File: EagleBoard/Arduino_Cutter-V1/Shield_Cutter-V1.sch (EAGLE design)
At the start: 83 parts, among them IC1 L298P, IC2 REG1117, K1 AQY21SOP, K2 AQY21SOP, U1 ARDUINOR3-DIMENSION, X1 2514-, X2 22-23-2041, X3 22-23-2021, X4 22-23-2021

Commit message: Feat: pcb routed
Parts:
- renumbered S1 to RESET
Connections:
- removed net N$25: SV9-1.S
- net BUTTON_INT: now also U1.D2; no longer U1.D3
- net DOWN_BUT: now also D12.C1, R26.2, U1.A1; no longer D11.C2, R25.2, U1.A2
- net E-STOP: now also SV9-1.S
- net LCD_D4: now also X1-8.KL; no longer X1-7.KL
- net LCD_D5: now also X1-7.KL; no longer X1-8.KL
- net LCD_D6: now also X1-10.KL; no longer X1-9.KL
- net LCD_D7: now also X1-9.KL; no longer X1-10.KL
- net RUN_BUT: now also D12.C2, R27.2, U1.A2; no longer D12.C1, R26.2, U1.A3
- net SELECT_BUT: now also D11.C2, R25.2, U1.A3; no longer D12.C2, R27.2, U1.A4/SDA
- net SOL_CUT: now also U1.A4/SDA; no longer U1.A0
- net SOL_PIERCE: now also U1.A5/SCL; no longer U1.A1
- net SPEED_POT: now also U1.A0; no longer U1.A5/SCL
- net STEPER1: now also U1.D10; no longer U1.D13
- net STEPER2: now also U1.D11; no longer U1.D12
- net STEPER3: now also U1.D12; no longer U1.D11
- net STEPER4: now also U1.D13; no longer U1.D10
- net UP_BUT: now also U1.D3; no longer U1.D2

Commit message: Feat: pcb routed
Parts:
- removed U$1: DISCLAIMER, SmartPrj:DISCLAIMER
- D11, D12: value (none) -> 40v
- R24: value (none) -> 10k
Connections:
- net GND: now also IC2.GND
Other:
- moved on the sheet: C1
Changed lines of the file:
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@@
 <part name="GND27" library="supply1" deviceset="GND" device=""/>
 <part name="GND28" library="supply1" deviceset="GND" device=""/>
-<part name="U$1" library="SmartPrj" deviceset="DISCLAIMER" device=""/>
 <part name="SUPPLY3" library="supply1" deviceset="GND" device=""/>
 <part name="SUPPLY1" library="supply1" deviceset="GND" device=""/>
@@
 <part name="P+16" library="supply1" deviceset="+5V" device=""/>
 <part name="R18" library="resistor" deviceset="R-US_" device="R0603" value="10kΩ"/>
-<part name="D11" library="zetex" library_urn="urn:adsk.eagle:library:418" deviceset="D_2C" device="SOT23"/>
-<part name="D12" library="zetex" library_urn="urn:adsk.eagle:library:418" deviceset="D_2C" device="SOT23"/>
+<part name="D11" library="zetex" library_urn="urn:adsk.eagle:library:418" deviceset="D_2C" device="SOT23" value="40v"/>
+<part name="D12" library="zetex" library_urn="urn:adsk.eagle:library:418" deviceset="D_2C" device="SOT23" value="40v"/>
 <part name="P+17" library="supply1" deviceset="+5V" device=""/>
 <part name="R19" library="resistor" deviceset="R-US_" device="M0805" value="10kΩ"/>
@@
 <part name="R21" library="resistor" deviceset="R-US_" device="R0603" value="10kΩ"/>
 <part name="R22" library="resistor" deviceset="R-US_" device="R0603" value="10kΩ"/>
-<part name="R24" library="pot" library_urn="urn:adsk.eagle:library:331" deviceset="TRIM_EU-" device="S64W"/>
+<part name="R24" library="pot" library_urn="urn:adsk.eagle:library:331" deviceset="TRIM_EU-" device="S64W" value="10k"/>
 <part name="P+5" library="supply1" deviceset="+5V" device=""/>
 <part name="GND20" library="supply1" deviceset="GND" device=""/>
@@
 <instance part="GND27" gate="1" x="132.08" y="81.28" rot="R180"/>
 <instance part="GND28" gate="1" x="167.64" y="81.28" rot="R180"/>
-<instance part="U$1" gate="G$1" x="-38.1" y="-104.14"/>
 <instance part="SUPPLY3" gate="1" x="-10.16" y="111.76"/>
 <instance part="SUPPLY1" gate="1" x="-25.4" y="111.76"/>
-<instance part="SUPPLY4" gate="1" x="2.54" y="111.76"/>
+<instance part="SUPPLY4" gate="1" x="5.08" y="111.76"/>
 <instance part="P+4" gate="1" x="17.78" y="132.08" smashed="yes">
 <attribute name="VALUE" x="19.685" y="134.62" size="1.778" layer="96" rot="R180"/>
@@
 </instance>
 <instance part="GND20" gate="1" x="157.48" y="-17.78"/>
-<instance part="C1" gate="G$1" x="2.54" y="121.92" smashed="yes">
-<attribute name="NAME" x="4.064" y="122.301" size="1.778" layer="95"/>
-<attribute name="VALUE" x="4.064" y="117.221" size="1.778" layer="96"/>
+<instance part="C1" gate="G$1" x="5.08" y="121.92" smashed="yes">
+<attribute name="NAME" x="6.604" y="122.301" size="1.778" layer="95"/>
+<attribute name="VALUE" x="6.604" y="117.221" size="1.778" layer="96"/>
 </instance>
 <instance part="C2" gate="G$1" x="17.78" y="121.92" smashed="yes">
@@
 </segment>
 <segment>
-<wire x1="2.54" y1="129.54" x2="17.78" y2="129.54" width="0.1524" layer="91"/>
-<wire x1="2.54" y1="124.46" x2="2.54" y2="129.54" width="0.1524" layer="91"/>
-<junction x="2.54" y="129.54"/>
+<wire x1="2.54" y1="129.54" x2="5.08" y2="129.54" width="0.1524" layer="91"/>
 <pinref part="P+4" gate="1" pin="+5V"/>
+<wire x1="5.08" y1="129.54" x2="17.78" y2="129.54" width="0.1524" layer="91"/>
 <wire x1="17.78" y1="124.46" x2="17.78" y2="129.54" width="0.1524" layer="91"/>
 <junction x="17.78" y="129.54"/>
-<pinref part="C1" gate="G$1" pin="1"/>
 <pinref part="C2" gate="G$1" pin="1"/>
 <pinref part="IC2" gate="G$1" pin="VOUT"/>
-<junction x="2.54" y="129.54"/>
+<pinref part="C1" gate="G$1" pin="1"/>
+<wire x1="5.08" y1="124.46" x2="5.08" y2="129.54" width="0.1524" layer="91"/>
+<junction x="5.08" y="129.54"/>
 </segment>
 <segment>
@@
 </segment>
 <segment>
-<wire x1="2.54" y1="116.84" x2="2.54" y2="114.3" width="0.1524" layer="91"/>
+<wire x1="5.08" y1="116.84" x2="5.08" y2="114.3" width="0.1524" layer="91"/>
 <pinref part="SUPPLY4" gate="1" pin="GND"/>
 <pinref part="C1" gate="G$1" pin="2"/>
@@
 </segment>
 <segment>
-<wire x1="-10.16" y1="116.84" x2="-10.16" y2="114.3" width="0.1524" layer="91"/>
-<pinref part="SUPPLY3" gate="1" pin="GND"/>
-</segment>
-<segment>
 <pinref part="C4" gate="G$1" pin="2"/>
 <pinref part="SUPPLY1" gate="1" pin="GND"/>
@@
 <pinref part="R30" gate="G$1" pin="1"/>
 <pinref part="GND35" gate="1" pin="GND"/>
+</segment>
+<segment>
+<pinref part="IC2" gate="G$1" pin="GND"/>
+<pinref part="SUPPLY3" gate="1" pin="GND"/>
+<wire x1="-10.16" y1="116.84" x2="-10.16" y2="114.3" width="0.1524" layer="91"/>
 </segment>
 </net>
@@
 <pinref part="R20" gate="G$1" pin="2"/>
 <wire x1="332.74" y1="157.48" x2="325.12" y2="157.48" width="0.1524" layer="91"/>
-<junction x="332.74" y="157.48"/>
-<wire x1="332.74" y1="157.48" x2="345.44" y2="157.48" width="0.1524" layer="91"/>
 <label x="335.28" y="157.48" size="1.778" layer="95"/>
 <pinref part="SV3" gate="-1" pin="S"/>
+<pinref part="SV9" gate="-1" pin="S"/>
+<wire x1="332.74" y1="157.48" x2="355.6" y2="157.48" width="0.1524" layer="91"/>
+<junction x="332.74" y="157.48"/>
 </segment>
 <segment>
@@
 <wire x1="259.08" y1="63.5" x2="259.08" y2="73.66" width="0.1524" layer="91"/>
 <label x="259.08" y="63.5" size="1.778" layer="95" rot="R90"/>
-</segment>
-<segment>
-<wire x1="345.44" y1="157.48" x2="355.6" y2="157.48" width="0.1524" layer="91"/>
-<pinref part="SV9" gate="-1" pin="S"/>
 </segment>
 </net>
@@
 </sheet>
 </sheets>
+<errors>
+</errors>
 </schematic>
 </drawing>

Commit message: FIX: increase components to 0805 size
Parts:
- C11, C2, C5, C6: device rcl:C-EUC0603 -> rcl:C-EUC0805
- C7: device SmartPrj:C-EUC0603K -> SmartPrj:C-EUC0805
- D11, D12: device zetex:D_2CSOT23 -> zetex:D_2CSOT323
- R10, R11, R12, R13, R14, R15, R16, R17, R18, R20, R21, R22, R23, R25, R26, R27, R28, R29, R3, R30, R4, R5, R6, R7, R8, R9: device resistor:R-US_R0603 -> resistor:R-US_R0805
- RESET: value (none) -> 1
- SV1, SV8, SV9: value (none) -> S3B-PH-K
- SV2, SV3, SV4, SV5, SV6, SV7: value (none) -> S2B-PH-K
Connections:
- net SELECT_BUT: now also D11.C1; no longer D11.C2
- net UP_BUT: now also D11.C2; no longer D11.C1
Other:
- moved on the sheet: C6, R24, X1-1, X1-10, X1-11, X1-12, X1-13, X1-14, X1-2, X1-3, X1-4, X1-5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

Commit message: Chore: gerbers and files for pcb manufacture
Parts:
- removed LED7: Green, led:LEDCHIPLED_0805
- removed R30: 1kΩ, resistor:R-US_R0805
- added X5: 22-23-2021, con-molex:22-23-2021
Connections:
- removed net N$18: LED7.C, R30.2
- removed net OUT5: C4.1, D10.K, IC2.VIN, LED7.A, SV2-2.S, U$2.TIP
- new net FUSE_RETURN: C4.1, D10.K, IC2.VIN, SV2-2.S, X5-2.S
- new net POWERIN: U$2.TIP, X5-1.S
- net GND: no longer R30.1
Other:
- moved on the sheet: C10, C6, C9, R24, RESET, SV2-1, SV2-2, VIN-CONNECT, X1-1, X1-10, X1-11, X1-12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

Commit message: Chore: add part names to pcb and cap from vmot to ground
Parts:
- removed C11: 100nF, rcl:C-EUC0805
- removed D12: 40v, zetex:D_2CSOT323
- removed LED1, LED2, LED3, LED4, LED5, LED6: Green, led:LEDCHIPLED_0805
- removed VIN-CONNECT: (no value), jumper:SJW
- added C3, C8: 100nF, rcl:C-EUC0805
- added D9: SS14, SmartPrj:SS14
- added FID4, FID5, FID6: FIDUCIALMOUNT, SmartPrj:FIDUCIALMOUNT
- added L1, L2, L3, L4, L5, L6: Green, led:LEDCHIPLED_0805
- added VIN: (no value), jumper:SJW
- C10, C9: value 10u 35V -> 100nF; device SmartPrj:C-EUC1210 -> rcl:C-EUC0805
- C2, C5: value 100nF -> 10u 35V; device rcl:C-EUC0805 -> SmartPrj:C-EUC1210
- C7: value 100n -> 100nF
- D10: value SS14 -> 40v; device SmartPrj:SS14 -> zetex:D_2CSOT323
- R10: value 2.5kΩ -> 10kΩ
- R11, R28: value 1kΩ -> 10Ω
- R13, R14, R15, R16: value 10kΩ -> 330Ω
- R19: device resistor:R-US_M0805 -> resistor:R-US_R0805
- R21: value 10kΩ -> 10Ω
- R22: device resistor:R-US_R0805 -> resistor:R-US_M0805
- R23, R25, R27, R3: value 10Ω -> 10kΩ
- R24: value 10k -> 10Ω; device pot:TRIM_EU-S64W -> resistor:R-US_R0805
- R29: value 1kΩ -> 10k; device resistor:R-US_R0805 -> pot:TRIM_EU-S64W
- R4: value 300Ω -> 10kΩ
- R5: value 10kΩ -> 1kΩ
- R6: value 2.5kΩ -> 1kΩ
- R7: value 10Ω -> 1kΩ
- R9: value 300Ω -> 10Ω
- SV1: value S3B-PH-K -> S2B-PH-K; device con-amp-mt:S03P -> con-amp-mt:S02P
- SV2: value S2B-PH-K -> S3B-PH-K; device con-amp-mt:S02P -> con-amp-mt:S03P
- X1: value 2514- -> 22-23-2021; device con-3m:2514- -> con-molex:22-23-2021
- X5: value 22-23-2021 -> 2514-; device con-molex:22-23-2021 -> con-3m:2514-
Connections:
- net +5V: now also C10.2, C3.1, C4.1, C8.1, R23.1, R25.1, R27.1, R29.A, R3.2, R4.1, SV2-2.S, VIN.2, X5-11.KL, X5-2.KL; no longer C1.1, C10.1, C11.1, C6.2, R13.1, R15.1, R16.1, R17.1, R21.2, R24.A, SV1-2.S, VIN-CONNECT.2, X1-11.KL, X1-2.KL
- net BUTTON_INT: now also D10.A, R22.2; no longer D12.A, R19.2
- net DOWN_BUT: now also D11.C1; no longer D12.C1
- net E-STOP: now also R19.2; no longer R20.2
- net ENABLEA: now also R3.1; no longer R21.1
- net ENABLEB: now also R4.2; no longer R22.2
- net ENCODER1: now also R17.2, R18.2, SV2-1.S; no longer R13.2, R14.2, SV1-1.S
- net FUSE_RETURN: now also C1.1, D9.K, SV1-2.S, X1-2.S; no longer C4.1, D10.K, SV2-2.S, X5-2.S
- net GND: now also C10.1, C3.2, C8.2, D9.A, L5.C, L6.C, R17.1, R29.E, R5.1, R6.1, R7.1, SV2-3.S, X5-1.KL, X5-12.KL, X5-5.KL; no longer C10.2, C11.2, D10.A, LED5.C, LED6.C, R11.1, R14.1, R24.E, R28.1, R29.1, SV1-3.S, X1-1.KL, X1-12.KL, X1-5.KL
- net LCD_D4: now also X5-8.KL; no longer X1-8.KL
- net LCD_D5: now also X5-7.KL; no longer X1-7.KL
- net LCD_D6: now also X5-10.KL; no longer X1-10.KL
- net LCD_D7: now also X5-9.KL; no longer X1-9.KL
- net LCD_EN: now also X5-6.KL; no longer X1-6.KL
- net LCD_RS: now also X5-4.KL; no longer X1-4.KL
- net N$1: now also L4.C; no longer LED4.C
- net N$10: now also R10.2; no longer R5.2
- net N$11: now also R11.1, R12.1; no longer R5.1, R7.1
- net N$12: now also L6.A, R16.2; no longer LED6.A, R4.2
- net N$13: now also R20.2, R21.1; no longer R15.2, R23.1
- net N$14: now also R15.2; no longer R6.2
- net N$15: now also R11.2; no longer R7.2
- net N$16: now also R10.1, R9.1; no longer R12.1, R3.1
- net N$17: now also R25.2; no longer R16.2
- net N$19: now also R27.2, R28.1; no longer R18.2, R27.1
- net N$2: now also L3.C, R7.2; no longer LED3.C, R11.2
- net N$3: now also L2.C, R6.2; no longer LED2.C, R28.2
- net N$4: now also L1.C, R5.2; no longer LED1.C, R29.2
- net N$5: now also R13.2; no longer R10.2
- net N$7: now also L5.A, R14.2; no longer LED5.A, R9.2
- net N$8: now also R9.2; no longer R3.2
- net N$9: now also R23.2, R24.1; no longer R17.2, R25.1
- net OUT1: now also L1.A; no longer LED1.A
- net OUT2: now also L2.A; no longer LED2.A
- net OUT3: now also L4.A; no longer LED4.A
- net OUT4: now also L3.A; no longer LED3.A
- net POWERIN: now also X1-1.S; no longer X5-1.S
- net RUN_BUT: now also D11.C2, R28.2; no longer D12.C2, R27.2
- net SELECT_BUT: now also D10.C1, R24.2; no longer D11.C1, R25.2
- net SOL_CUT: now also R13.1, R14.1; no longer R10.1, R9.1
- net SOL_PIERCE: now also R15.1, R16.1; no longer R4.1, R6.1
- net UP_BUT: now also D10.C2, R21.2; no longer D11.C2, R23.2
- net V0: now also R29.S, X5-3.KL; no longer R24.S, X1-3.KL
- net VIN: now also VIN.1; no longer VIN-CONNECT.1
- net VMOT: now also C6.2, SV1-1.S; no longer SV2-1.S
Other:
- moved on the sheet: C1, C10, C2, C4, C5, C6, C7, C9, D1, D11, D2, D3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

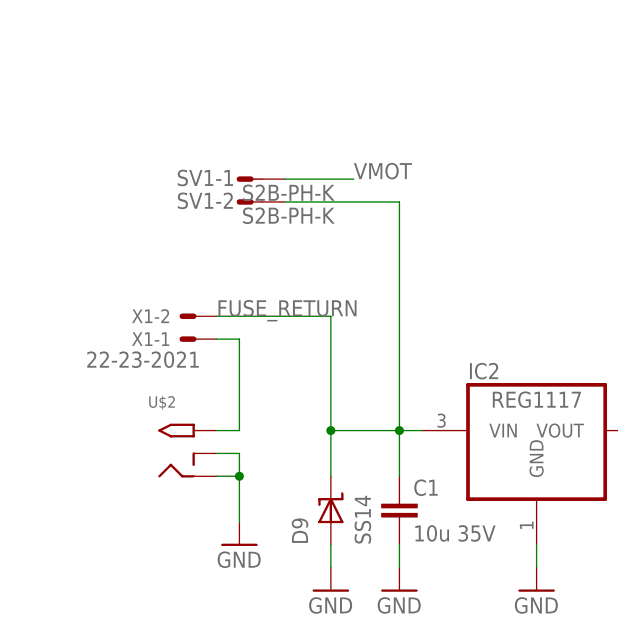
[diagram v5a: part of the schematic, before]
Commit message: Fix: fix floating ground. Feat: add power input terminal.
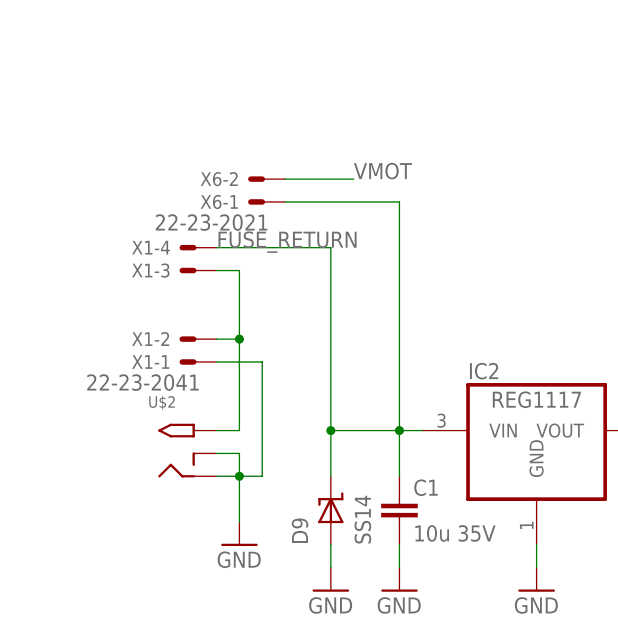
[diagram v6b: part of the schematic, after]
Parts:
- removed SV1: S2B-PH-K, con-amp-mt:S02P
- added X6: 22-23-2021, con-molex:22-23-2021
- X1: value 22-23-2021 -> 22-23-2041; device con-molex:22-23-2021 -> con-molex:22-23-2041
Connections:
- net FUSE_RETURN: now also X1-4.S, X6-1.S; no longer SV1-2.S, X1-2.S
- net GND: now also X1-1.S
- net POWERIN: now also X1-2.S, X1-3.S; no longer X1-1.S
- net VMOT: now also X6-2.S; no longer SV1-1.S
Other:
- moved on the sheet: X1-1, X1-2

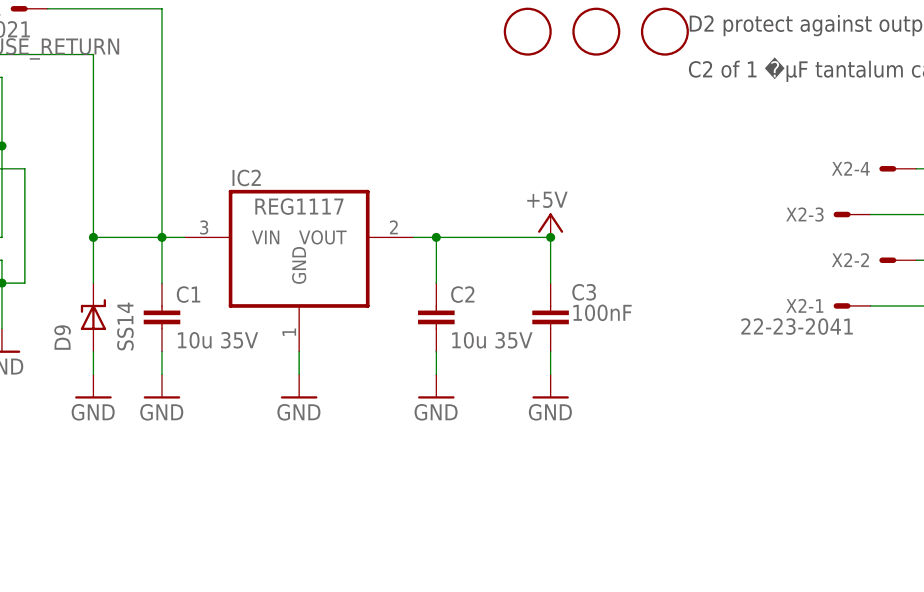
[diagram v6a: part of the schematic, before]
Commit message: Feat: add fuse to 5v power
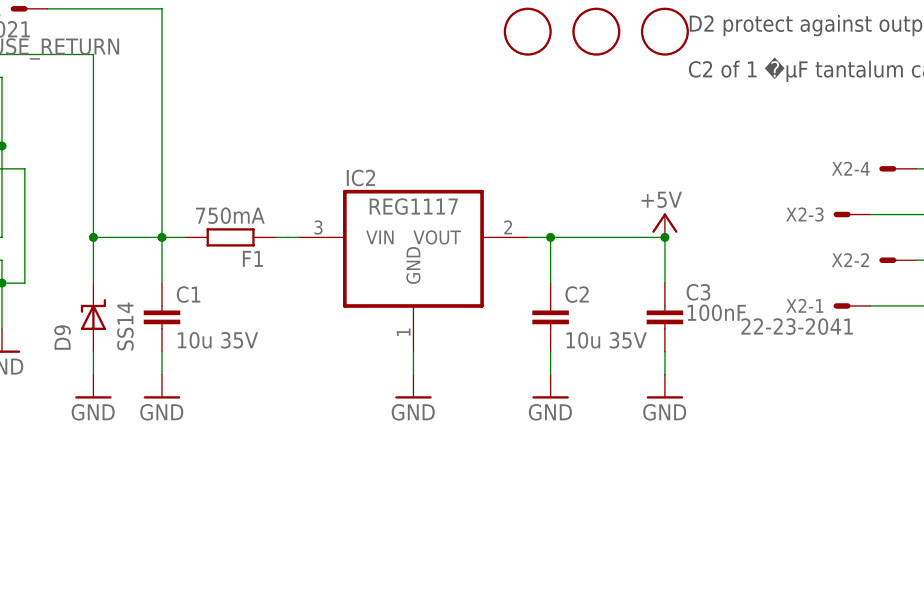
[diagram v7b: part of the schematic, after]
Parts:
- added F1: 750mA, SmartPrj:R-EU_R1206
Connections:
- new net N$18: F1.1, IC2.VIN
- net FUSE_RETURN: now also F1.2; no longer IC2.VIN
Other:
- moved on the sheet: C2, C3, IC2
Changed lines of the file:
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@@
 <part name="X6" library="con-molex" library_urn="urn:adsk.eagle:library:165" deviceset="22-23-2021" device=""/>
 <part name="X1" library="con-molex" library_urn="urn:adsk.eagle:library:165" deviceset="22-23-2041" device=""/>
+<part name="F1" library="SmartPrj" deviceset="R-EU_" device="R1206" value="750mA"/>
 </parts>
 <sheets>
@@
 <instance part="GND27" gate="1" x="30.48" y="7.62" rot="R180"/>
 <instance part="GND28" gate="1" x="66.04" y="7.62" rot="R180"/>
-<instance part="SUPPLY3" gate="1" x="-111.76" y="38.1"/>
+<instance part="SUPPLY3" gate="1" x="-99.06" y="38.1"/>
 <instance part="SUPPLY1" gate="1" x="-127" y="38.1"/>
-<instance part="SUPPLY4" gate="1" x="-96.52" y="38.1"/>
-<instance part="P+4" gate="1" x="-83.82" y="58.42" smashed="yes">
-<attribute name="VALUE" x="-81.915" y="60.96" size="1.778" layer="96" rot="R180"/>
+<instance part="SUPPLY4" gate="1" x="-83.82" y="38.1"/>
+<instance part="P+4" gate="1" x="-71.12" y="58.42" smashed="yes">
+<attribute name="VALUE" x="-69.215" y="60.96" size="1.778" layer="96" rot="R180"/>
 </instance>
 <instance part="P+9" gate="1" x="-96.52" y="-7.62" smashed="yes">
@@
 <attribute name="VALUE" x="245.745" y="91.44" size="1.778" layer="96" rot="R180"/>
 </instance>
-<instance part="SUPPLY5" gate="1" x="-83.82" y="38.1"/>
+<instance part="SUPPLY5" gate="1" x="-71.12" y="38.1"/>
 <instance part="X5" gate="-1" x="-60.96" y="-50.8"/>
 <instance part="X5" gate="-2" x="-60.96" y="-53.34"/>
@@
 </instance>
 <instance part="GND20" gate="1" x="-30.48" y="-66.04"/>
-<instance part="C2" gate="G$1" x="-96.52" y="48.26" smashed="yes">
-<attribute name="NAME" x="-94.996" y="48.641" size="1.778" layer="95"/>
-<attribute name="VALUE" x="-94.996" y="43.561" size="1.778" layer="96"/>
-</instance>
-<instance part="C3" gate="G$1" x="-83.82" y="48.26" smashed="yes">
-<attribute name="NAME" x="-81.534" y="48.895" size="1.778" layer="95"/>
-<attribute name="VALUE" x="-81.534" y="46.609" size="1.778" layer="96"/>
+<instance part="C2" gate="G$1" x="-83.82" y="48.26" smashed="yes">
+<attribute name="NAME" x="-82.296" y="48.641" size="1.778" layer="95"/>
+<attribute name="VALUE" x="-82.296" y="43.561" size="1.778" layer="96"/>
+</instance>
+<instance part="C3" gate="G$1" x="-71.12" y="48.26" smashed="yes">
+<attribute name="NAME" x="-68.834" y="48.895" size="1.778" layer="95"/>
+<attribute name="VALUE" x="-68.834" y="46.609" size="1.778" layer="96"/>
 </instance>
 <instance part="C8" gate="G$1" x="177.8" y="73.66" smashed="yes">
@@
 </instance>
 <instance part="L5" gate="G$1" x="129.54" y="83.82" rot="R270"/>
-<instance part="IC2" gate="G$1" x="-111.76" y="55.88"/>
+<instance part="IC2" gate="G$1" x="-99.06" y="55.88"/>
 <instance part="C1" gate="G$1" x="-127" y="48.26" smashed="yes">
 <attribute name="NAME" x="-125.476" y="48.641" size="1.778" layer="95"/>
@@
 <instance part="X1" gate="-3" x="-149.86" y="73.66" rot="R180"/>
 <instance part="X1" gate="-4" x="-149.86" y="76.2" rot="R180"/>
+<instance part="F1" gate="G$1" x="-119.38" y="55.88" rot="R180"/>
 </instances>
 <busses>
@@
 </segment>
 <segment>
-<wire x1="-99.06" y1="55.88" x2="-96.52" y2="55.88" width="0.1524" layer="91"/>
+<wire x1="-86.36" y1="55.88" x2="-83.82" y2="55.88" width="0.1524" layer="91"/>
 <pinref part="P+4" gate="1" pin="+5V"/>
-<wire x1="-96.52" y1="55.88" x2="-83.82" y2="55.88" width="0.1524" layer="91"/>
-<wire x1="-83.82" y1="50.8" x2="-83.82" y2="55.88" width="0.1524" layer="91"/>
-<junction x="-83.82" y="55.88"/>
+<wire x1="-83.82" y1="55.88" x2="-71.12" y2="55.88" width="0.1524" layer="91"/>
+<wire x1="-71.12" y1="50.8" x2="-71.12" y2="55.88" width="0.1524" layer="91"/>
+<junction x="-71.12" y="55.88"/>
 <pinref part="C3" gate="G$1" pin="1"/>
 <pinref part="IC2" gate="G$1" pin="VOUT"/>
 <pinref part="C2" gate="G$1" pin="1"/>
-<wire x1="-96.52" y1="50.8" x2="-96.52" y2="55.88" width="0.1524" layer="91"/>
-<junction x="-96.52" y="55.88"/>
+<wire x1="-83.82" y1="50.8" x2="-83.82" y2="55.88" width="0.1524" layer="91"/>
+<junction x="-83.82" y="55.88"/>
 </segment>
 <segment>
@@
 </segment>
 <segment>
-<wire x1="-96.52" y1="43.18" x2="-96.52" y2="40.64" width="0.1524" layer="91"/>
+<wire x1="-83.82" y1="43.18" x2="-83.82" y2="40.64" width="0.1524" layer="91"/>
 <pinref part="SUPPLY4" gate="1" pin="GND"/>
 <pinref part="C2" gate="G$1" pin="2"/>
@@
 <segment>
 <pinref part="SUPPLY5" gate="1" pin="GND"/>
-<wire x1="-83.82" y1="40.64" x2="-83.82" y2="43.18" width="0.1524" layer="91"/>
+<wire x1="-71.12" y1="40.64" x2="-71.12" y2="43.18" width="0.1524" layer="91"/>
 <pinref part="C3" gate="G$1" pin="2"/>
 </segment>
@@
 <pinref part="IC2" gate="G$1" pin="GND"/>
 <pinref part="SUPPLY3" gate="1" pin="GND"/>
-<wire x1="-111.76" y1="43.18" x2="-111.76" y2="40.64" width="0.1524" layer="91"/>
+<wire x1="-99.06" y1="43.18" x2="-99.06" y2="40.64" width="0.1524" layer="91"/>
 </segment>
 <segment>
@@
 <segment>
 <junction x="-127" y="55.88"/>
-<pinref part="IC2" gate="G$1" pin="VIN"/>
-<wire x1="-127" y1="55.88" x2="-124.46" y2="55.88" width="0.1524" layer="91"/>
 <pinref part="C1" gate="G$1" pin="1"/>
 <wire x1="-127" y1="50.8" x2="-127" y2="55.88" width="0.1524" layer="91"/>
@@
 <pinref part="X6" gate="-1" pin="S"/>
 <pinref part="X1" gate="-4" pin="S"/>
+<pinref part="F1" gate="G$1" pin="2"/>
+<wire x1="-124.46" y1="55.88" x2="-127" y2="55.88" width="0.1524" layer="91"/>
 </segment>
 </net>
@@
 </segment>
 </net>
+<net name="N$18" class="0">
+<segment>
+<pinref part="F1" gate="G$1" pin="1"/>
+<pinref part="IC2" gate="G$1" pin="VIN"/>
+<wire x1="-114.3" y1="55.88" x2="-111.76" y2="55.88" width="0.1524" layer="91"/>
+</segment>
+</net>
